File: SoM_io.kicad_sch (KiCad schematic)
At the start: 16 parts, among them J1 Hermaphroditic_Molex_203456-0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, U14 NTS0102_XSON, U15 NTS0102_XSON, U16 NTS0102_XSON, U17 NTS0102_XSON, U4 NTS0102_XSON

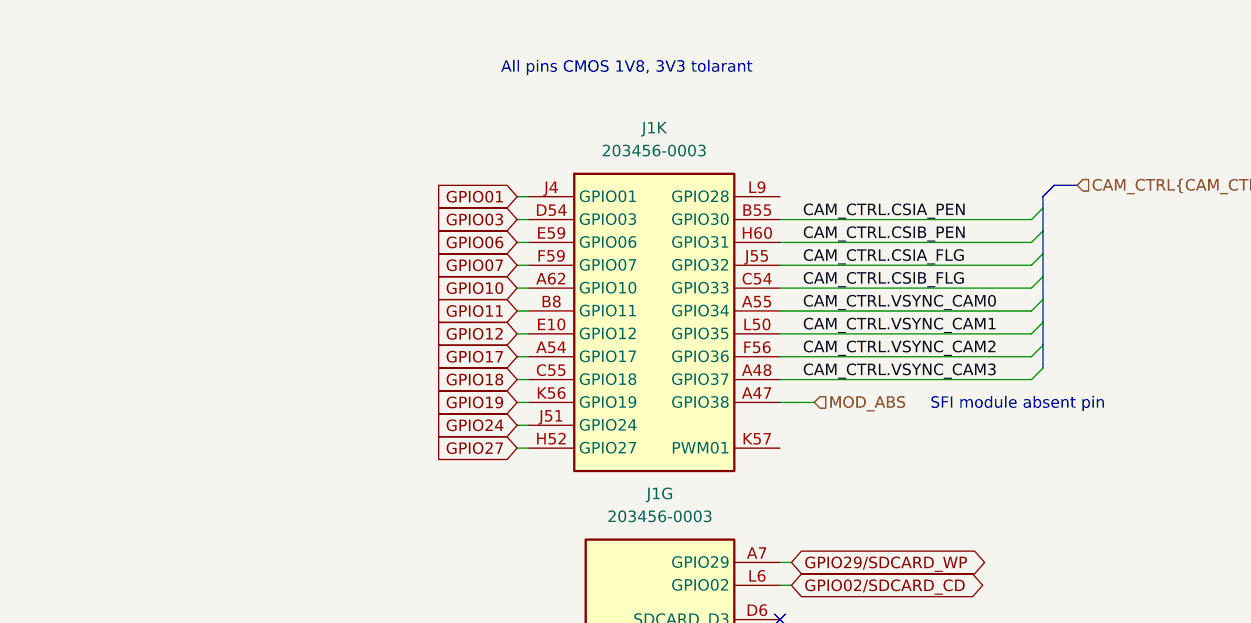
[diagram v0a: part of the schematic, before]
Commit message: [#81970] Route present on root GPIO pins on CSI and Peripherals sheets
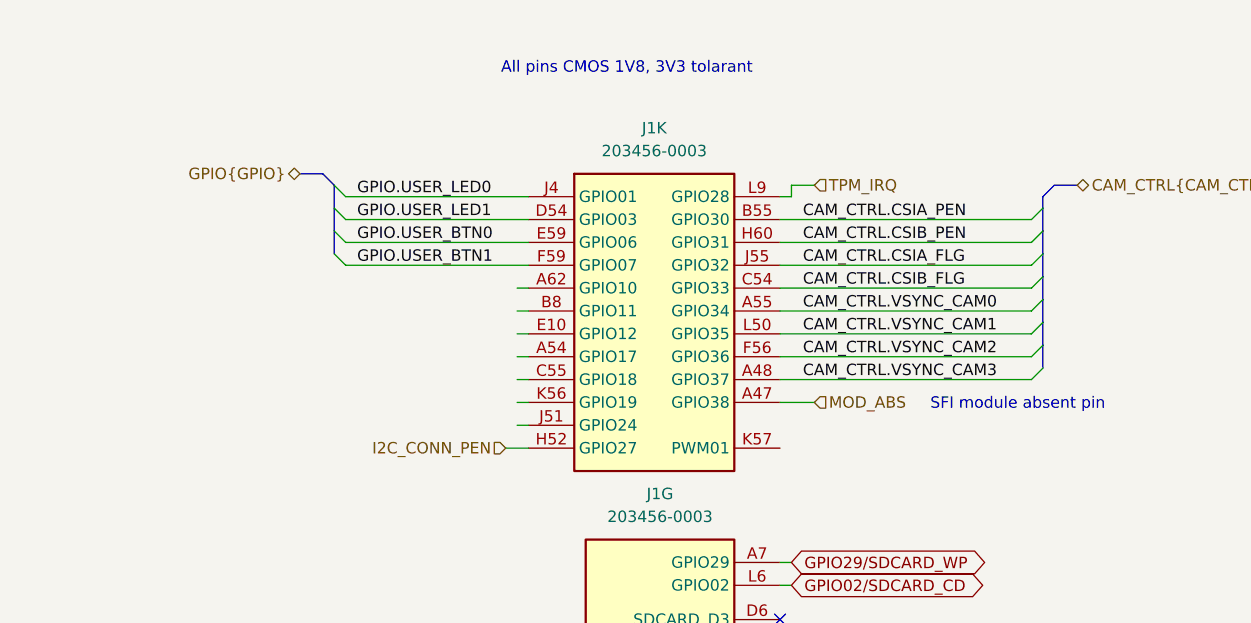
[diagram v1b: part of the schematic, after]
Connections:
- net TPM_IRQ: now reaches J1.L9 (GPIO28)
- net GPIO01 renamed GPIO.USER_LED0
- net GPIO03 renamed GPIO.USER_LED1
- net GPIO06 renamed GPIO.USER_BTN0
- net GPIO07 renamed GPIO.USER_BTN1
- net GPIO10: no longer names the net of J1.A62 (GPIO10)
- net GPIO11: no longer names the net of J1.B8 (GPIO11)
- net GPIO12: no longer names the net of J1.E10 (GPIO12)
- net GPIO17: no longer names the net of J1.A54 (GPIO17)
- net GPIO18: no longer names the net of J1.C55 (GPIO18)
- net GPIO19: no longer names the net of J1.K56 (GPIO19)
- net GPIO24: no longer names the net of J1.J51 (GPIO24)
- net GPIO27 renamed I2C_CONN_PEN

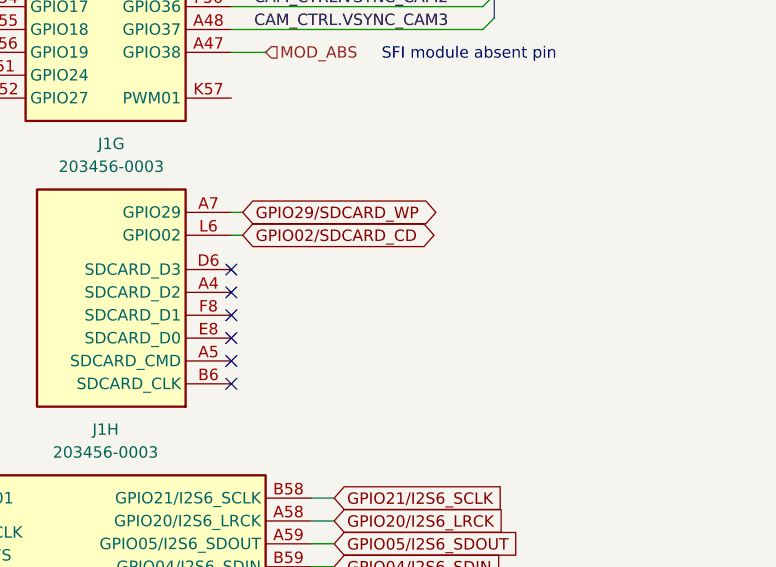
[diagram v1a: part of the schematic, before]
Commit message: [#82057] Route SDIO
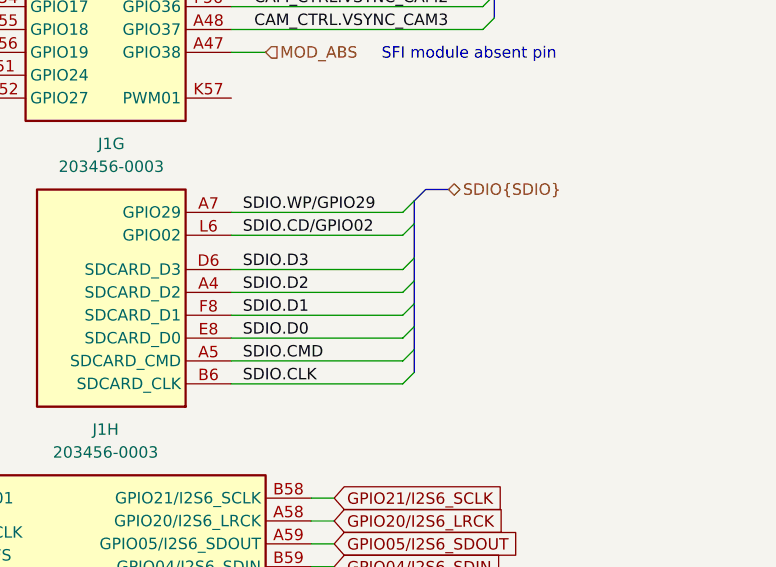
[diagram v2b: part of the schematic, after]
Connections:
- net SDIO.D2: now reaches J1.A4 (SDCARD_D2)
- net SDIO.CMD: now reaches J1.A5 (SDCARD_CMD)
- net SDIO.CLK: now reaches J1.B6 (SDCARD_CLK)
- net SDIO.D3: now reaches J1.D6 (SDCARD_D3)
- net SDIO.D0: now reaches J1.E8 (SDCARD_D0)
- net SDIO.D1: now reaches J1.F8 (SDCARD_D1)
- net GPIO02/SDCARD_CD renamed SDIO.CD/GPIO02
- net GPIO29/SDCARD_WP renamed SDIO.WP/GPIO29
- no-connect marks 6 -> 0

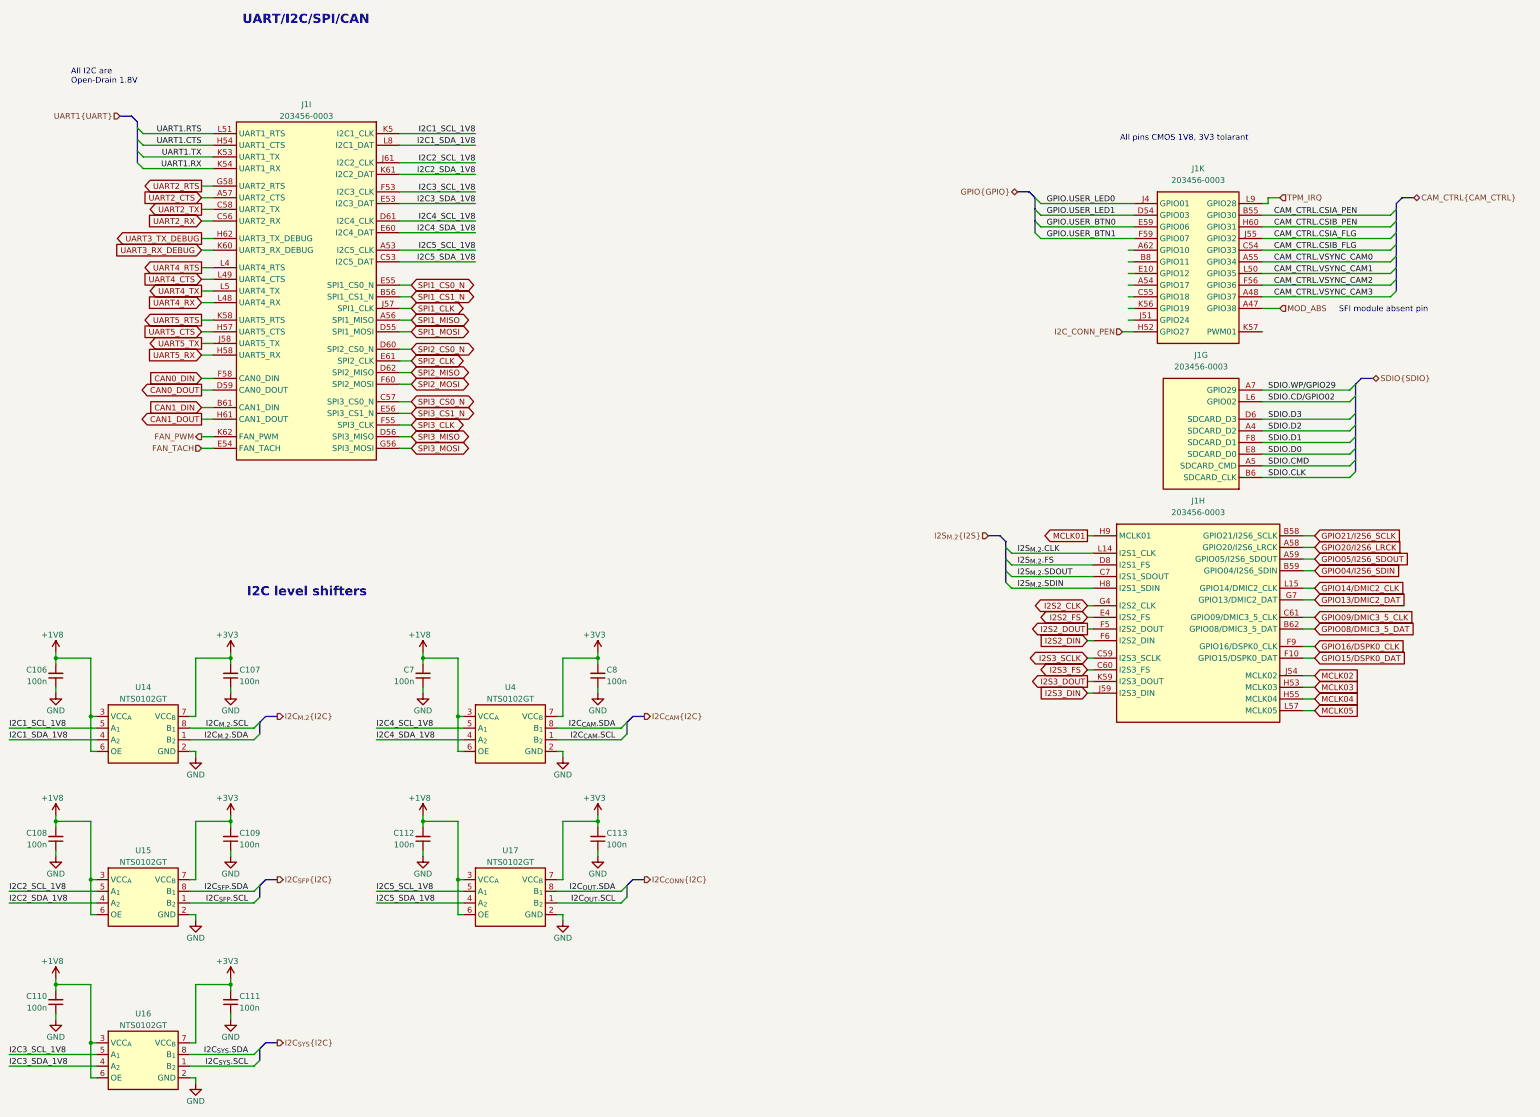
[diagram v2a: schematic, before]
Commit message: [#82057] Route UART, SPI, I2S and unused GPIO on SoM and Expansion connector schematics
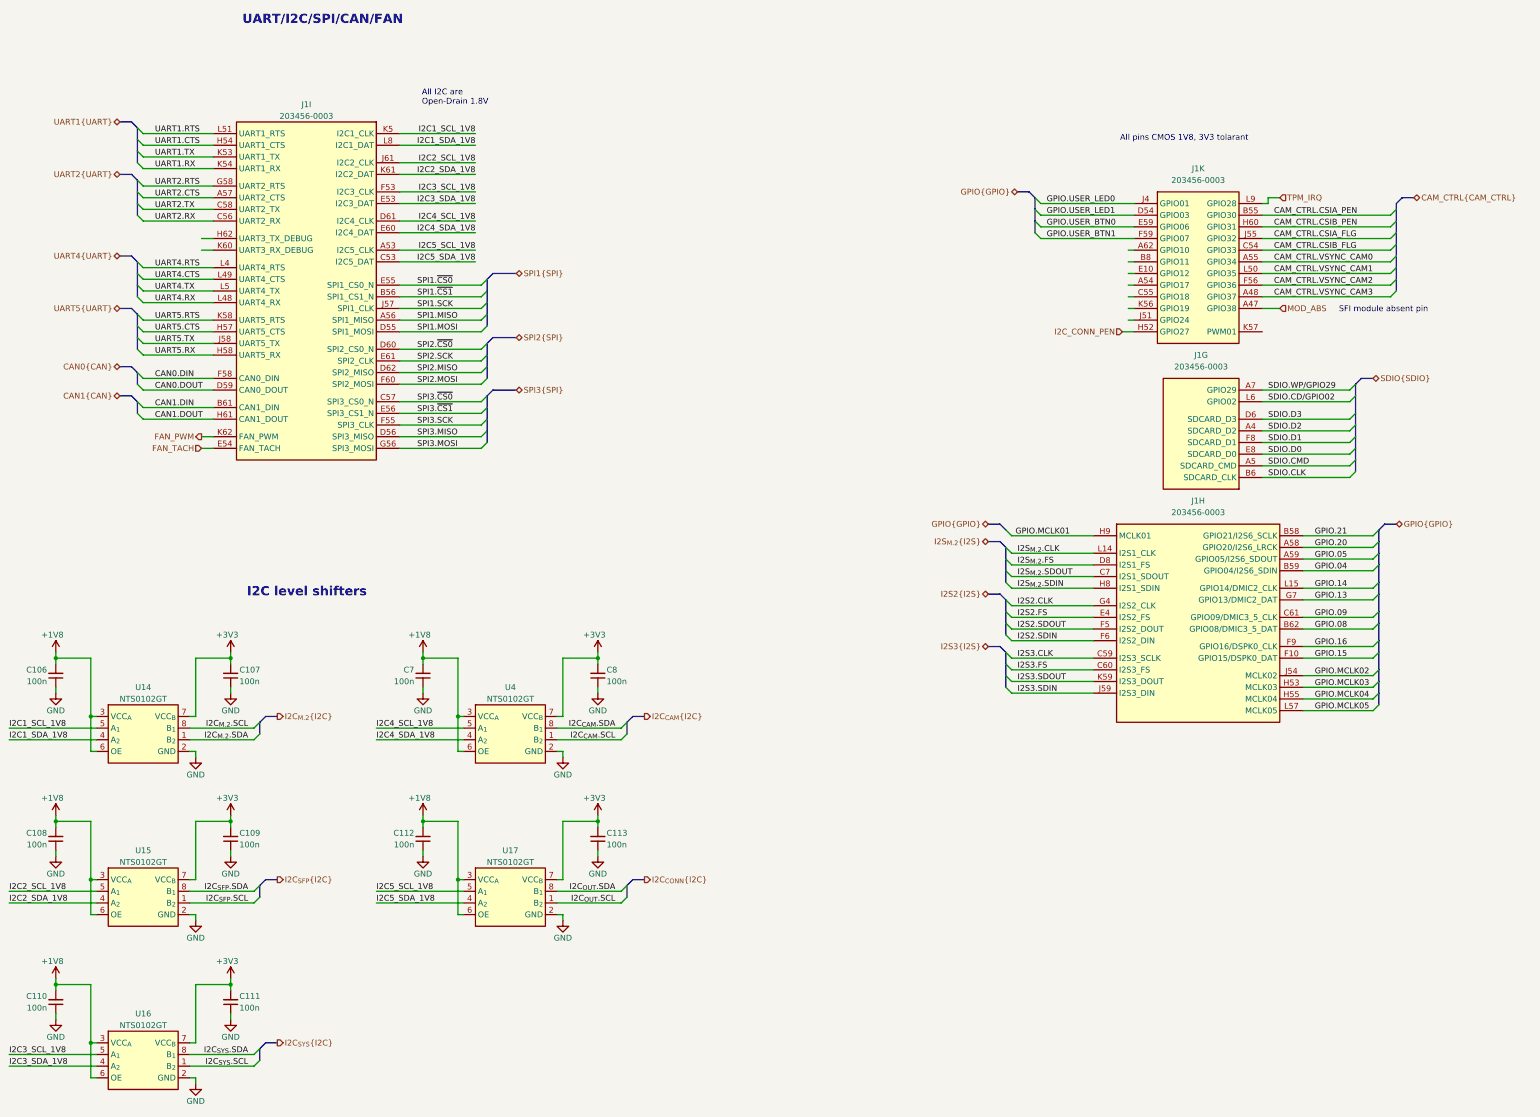
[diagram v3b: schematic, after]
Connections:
- net CAN0_DIN renamed CAN0.DIN
- net CAN0_DOUT renamed CAN0.DOUT
- net CAN1_DIN renamed CAN1.DIN
- net CAN1_DOUT renamed CAN1.DOUT
- net GPIO04/I2S6_SDIN renamed GPIO.04
- net GPIO05/I2S6_SDOUT renamed GPIO.05
- net GPIO08/DMIC3_5_DAT renamed GPIO.08
- net GPIO09/DMIC3_5_CLK renamed GPIO.09
- net GPIO13/DMIC2_DAT renamed GPIO.13
- net GPIO14/DMIC2_CLK renamed GPIO.14
- net GPIO15/DSPK0_DAT renamed GPIO.15
- net GPIO16/DSPK0_CLK renamed GPIO.16
- net GPIO20/I2S6_LRCK renamed GPIO.20
- net GPIO21/I2S6_SCLK renamed GPIO.21
- net I2S2_CLK renamed I2S2.CLK
- net I2S2_DIN renamed I2S2.SDIN
- net I2S2_DOUT renamed I2S2.SDOUT
- net I2S2_FS renamed I2S2.FS
- net I2S3_DIN renamed I2S3.SDIN
- net I2S3_DOUT renamed I2S3.SDOUT
- net I2S3_FS renamed I2S3.FS
- net I2S3_SCLK renamed I2S3.CLK
- net MCLK01 renamed GPIO.MCLK01
- net MCLK02 renamed GPIO.MCLK02
- net MCLK03 renamed GPIO.MCLK03
- net MCLK04 renamed GPIO.MCLK04
- net MCLK05 renamed GPIO.MCLK05
- net SPI1_CLK renamed SPI1.SCK
- net SPI1_CS0_N renamed SPI1.~{CS0}
- net SPI1_CS1_N renamed SPI1.~{CS1}
- net SPI1_MISO renamed SPI1.MISO
- net SPI1_MOSI renamed SPI1.MOSI
- net SPI2_CLK renamed SPI2.SCK
- net SPI2_CS0_N renamed SPI2.~{CS0}
- net SPI2_MISO renamed SPI2.MISO
- net SPI2_MOSI renamed SPI2.MOSI
- net SPI3_CLK renamed SPI3.SCK
- net SPI3_CS0_N renamed SPI3.~{CS0}
- net SPI3_CS1_N renamed SPI3.~{CS1}
- net SPI3_MISO renamed SPI3.MISO
- net SPI3_MOSI renamed SPI3.MOSI
- net UART2_CTS renamed UART2.CTS
- net UART2_RTS renamed UART2.RTS
- net UART2_RX renamed UART2.RX
- net UART2_TX renamed UART2.TX
- net UART3_RX_DEBUG: no longer names the net of J1.K60 (UART3_RX_DEBUG)
- net UART3_TX_DEBUG: no longer names the net of J1.H62 (UART3_TX_DEBUG)
- net UART4_CTS renamed UART4.CTS
- net UART4_RTS renamed UART4.RTS
- net UART4_RX renamed UART4.RX
- net UART4_TX renamed UART4.TX
- net UART5_CTS renamed UART5.CTS
- net UART5_RTS renamed UART5.RTS
- net UART5_RX renamed UART5.RX
- net UART5_TX renamed UART5.TX
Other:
- note added: "UART/I2C/SPI/CAN/FAN"
- note removed: "UART/I2C/SPI/CAN"

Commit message: [#82757] Rename project to jetson-agx-thor-baseboard
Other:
- title: Jetson Orin AGX Baseboard -> Jetson AGX Thor Baseboard
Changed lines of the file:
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@@
 	(paper "A3")
 	(title_block
-		(title "Jetson Orin AGX Baseboard")
+		(title "Jetson AGX Thor Baseboard")
 		(date "2025-08-11")
 		(rev "1.0.0")

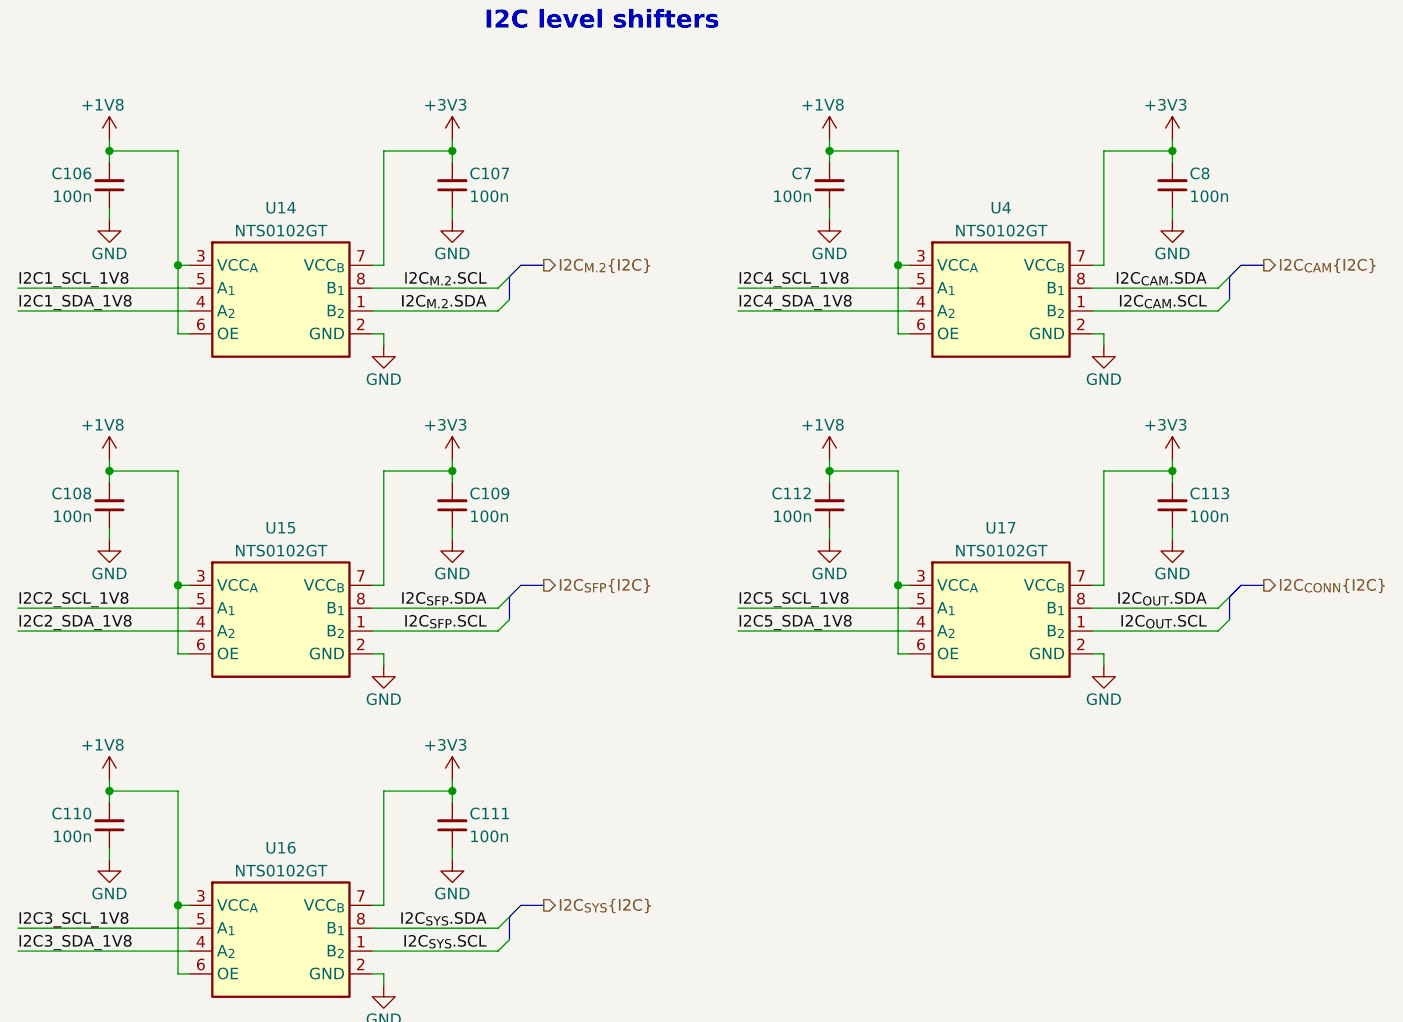
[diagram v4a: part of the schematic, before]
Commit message: [#82757] Cleanup: reorganise page numbers and fix annotations
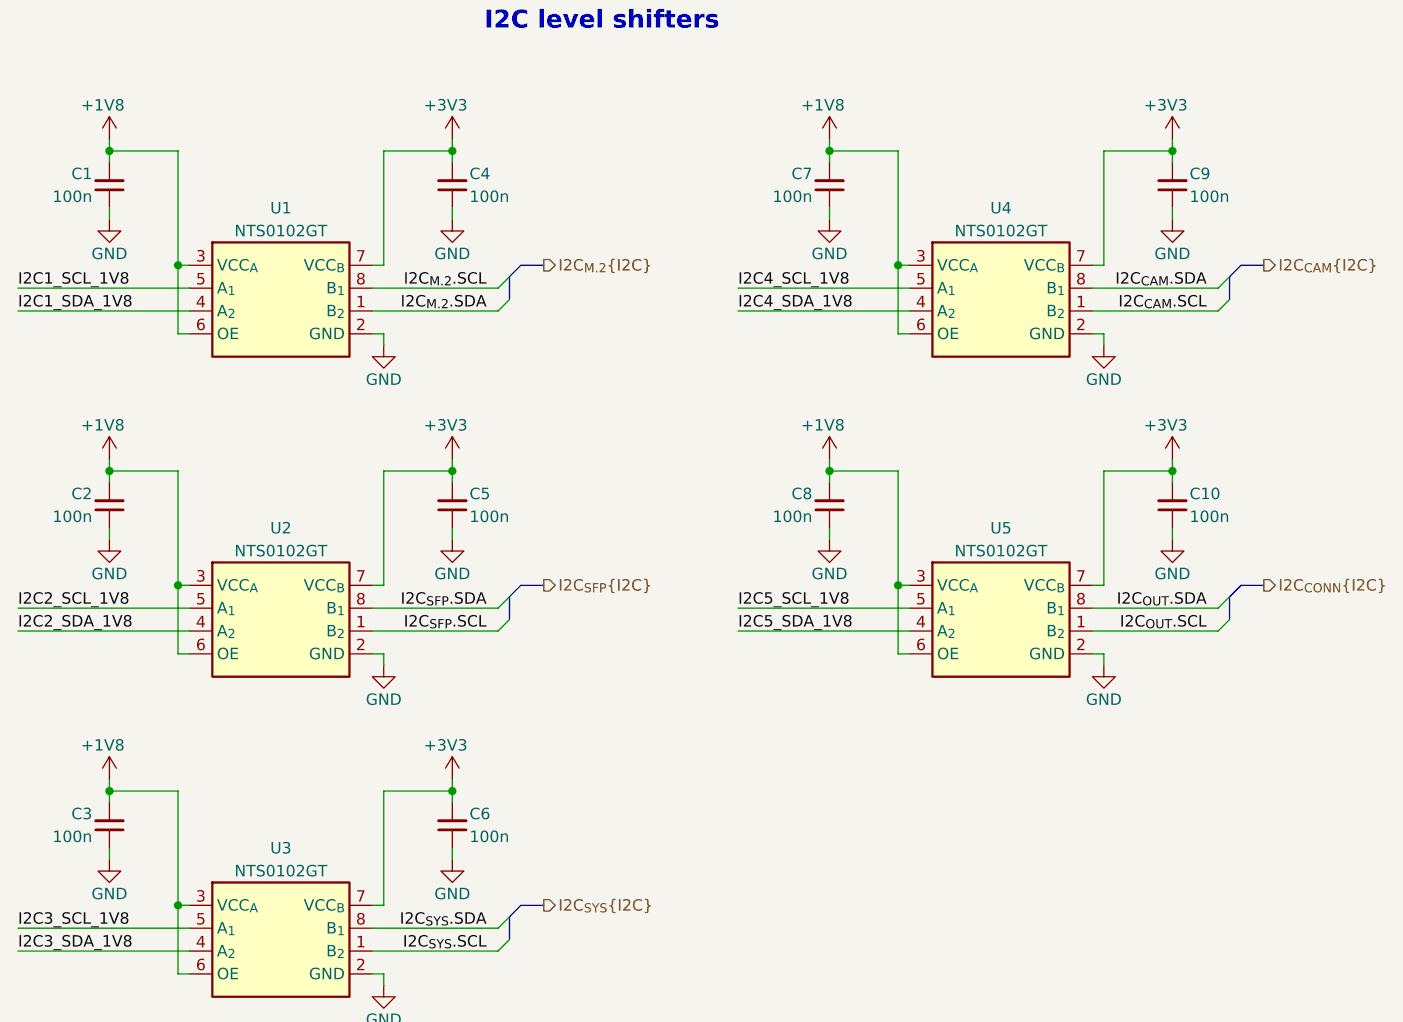
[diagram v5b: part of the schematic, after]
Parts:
- renumbered C106 to C1, C113 to C10, C108 to C2, C110 to C3, C107 to C4, C109 to C5, C111 to C6, C112 to C8, C8 to C9, U14 to U1, U15 to U2, U16 to U3, U17 to U5
